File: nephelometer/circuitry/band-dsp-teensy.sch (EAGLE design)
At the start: 23 parts, among them IC1 AD822N, IC4 LM4041CILP, T1 2N2222, T2 2N2222

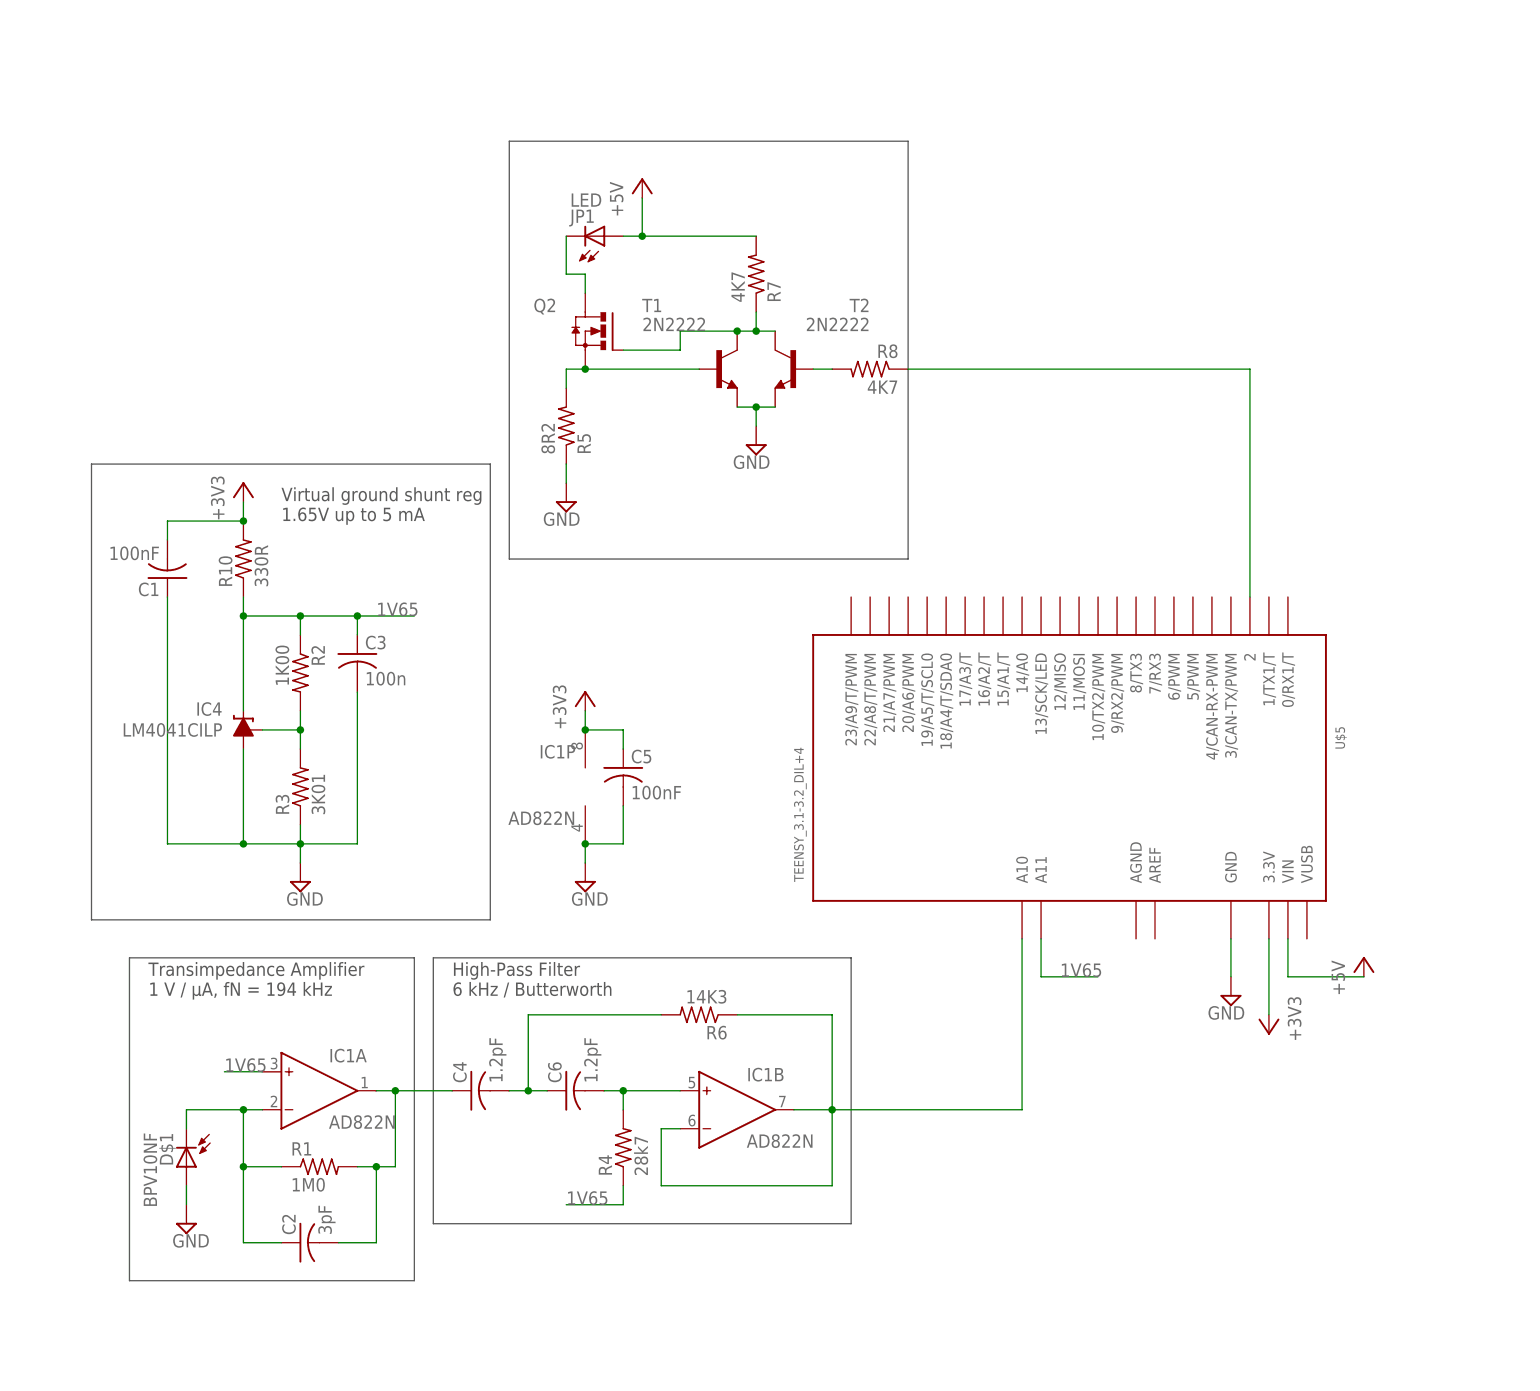
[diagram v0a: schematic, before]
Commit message: programmable gain amplifier incorporated
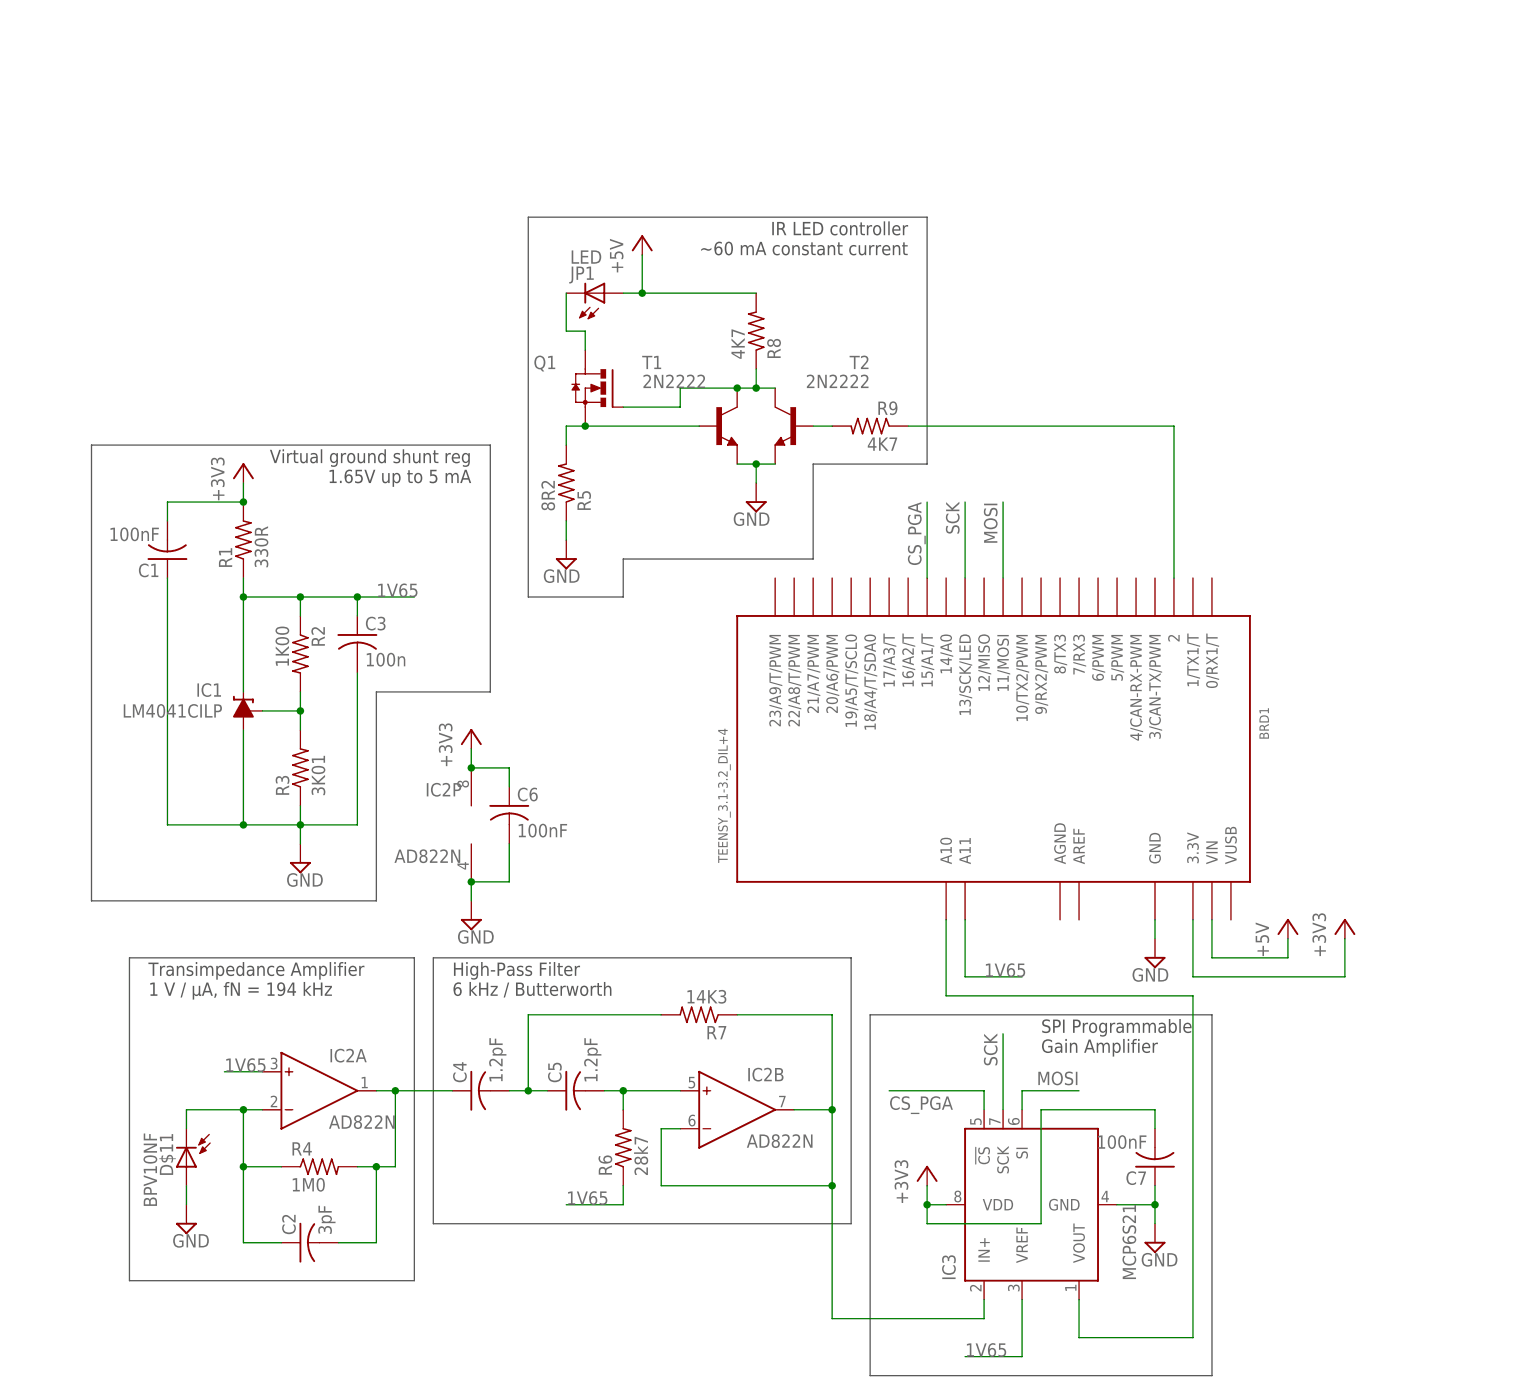
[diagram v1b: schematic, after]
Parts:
- removed IC4: LM4041CILP, texas:LM4041CILP
- removed Q2: (no value), ingolia:IRLB8721
- removed R10: 330R, adafruit:R-US_0207/9
- removed U$5: TEENSY_3.1-3.2_DIL+4, Teensy_3_and_LC_Series_Boards_v1.4:TEENSY_3.1-3.2_DIL+4
- added BRD1: TEENSY_3.1-3.2_DIL+4, Teensy_3_and_LC_Series_Boards_v1.4:TEENSY_3.1-3.2_DIL+4
- added C7: 100nF, adafruit:C-US025-025X050
- added IC2: AD822N, analog-devices:AD822N
- added IC3: MCP6S21, ingolia:MCP6S21
- added Q1: (no value), ingolia:IRLB8721
- added R9: 4K7, adafruit:R-US_0207/9
- C5: value 100nF -> 1.2pF; DIGIKEY# BC1084CT-ND -> BC1026CT-ND; MANF (none) -> Vishay BC Components; MANF# (none) -> K122J15C0GF5TL2
- C6: value 1.2pF -> 100nF; DIGIKEY# BC1026CT-ND -> BC1084CT-ND; MANF Vishay BC Components -> (none); MANF# K122J15C0GF5TL2 -> (none)
- IC1: value AD822N -> LM4041CILP; device analog-devices:AD822N -> texas:LM4041CILP; DIGIKEY# AD823ANZ-ND -> 296-22173-1-ND; MANF Analog Devices Inc. -> Texas Instruments; MANF# AD823ANZ -> LM4041CILPR
- R1: value 1M0 -> 330R; DIGIKEY# RNV14FAL1M00CT-ND -> CF14JT330RCT-ND; MANF Stackpole Electronics Inc -> Stackpole Electronics Inc.; MANF# RNV14FAL1M00 -> CF14JT330R
- R4: value 28k7 -> 1M0; DIGIKEY# 28.7KXBK-ND -> RNV14FAL1M00CT-ND; MANF Yageo -> Stackpole Electronics Inc; MANF# MFR-25FBF52-28K7 -> RNV14FAL1M00
- R6: value 14K3 -> 28k7; DIGIKEY# 14.3KXBK-ND -> 28.7KXBK-ND; MANF# MFR-25FBF52-14K3 -> MFR-25FBF52-28K7
- R7: value 4K7 -> 14K3; DIGIKEY# CF14JT4K70CT-ND -> 14.3KXBK-ND; MANF Stackpole Electronics Inc -> Yageo; MANF# CF14JT4K70 -> MFR-25FBF52-14K3
- renumbered D$1 to D$11
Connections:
- removed net N$10: IC1B.IN-, IC1B.OUT, R6.1, U$5.A10
- new net CS_PGA: BRD1.15/A1/T, IC3.!CS
- new net MOSI: BRD1.11/MOSI, IC3.SI
- new net N$3: IC2B.IN-, IC2B.OUT, IC3.IN+, R7.1
- new net N$4: BRD1.A10, IC3.VOUT
- new net SCK: BRD1.13/SCK/LED, IC3.SCK
- net +3V3: now also BRD1.3.3V, C6.1, C7.2, IC2P.V+, IC3.VDD, R1.2; no longer C5.1, IC1P.V+, R10.2, U$5.3.3V
- net +5V: now also BRD1.VIN, R8.2; no longer R7.2, U$5.VIN
- net 1V65: now also BRD1.A11, IC1.C, IC2A.IN+, IC3.VREF, R1.1, R6.1; no longer IC1A.IN+, IC4.C, R10.1, R4.1, U$5.A11
- net GND: now also BRD1.GND, C6.2, C7.1, IC1.A, IC2P.V-, IC3.GND; no longer C5.2, IC1P.V-, IC4.A, U$5.GND
- net LEDCTRL: now also R9.2; no longer R8.2
- net N$1: now also IC2A.IN-, R4.1; no longer IC1A.IN-, R1.1
- net N$14: now also Q1.S; no longer Q2.S
- net N$18: now also Q1.D; no longer Q2.D
- net N$2: now also C5.1, R7.2; no longer C6.1, R6.2
- net N$22: now also IC2A.OUT, R4.2; no longer IC1A.OUT, R1.2
- net N$35: now also IC1.FB; no longer IC4.FB
- net N$5: now also BRD1.2, R9.1; no longer R8.1, U$5.2
- net N$8: now also Q1.G, R8.1; no longer Q2.G, R7.1
- net N$9: now also C5.2, IC2B.IN+, R6.2; no longer C6.2, IC1B.IN+, R4.2
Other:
- note added: "IR LED controller ~60 mA constant current"
- note added: "SPI Programmable Gain Amplifier"
- moved on the sheet: C1, C3, C5, C6, JP1, R1, R2, R3, R4, R5, R6, R7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

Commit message: Stackable motor controller board w/ 3.3V control; USB versus wall power; test order for components
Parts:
- added D1, D2: 1N5817-T, diode:1N5817-T
- added J1: RJ11-6PTH, SparkFun-Connectors:RJ11-6PTH
- added R10, R11: 330R, adafruit:R-US_0207/9
- added R12: 150R, adafruit:R-US_0207/9
- added U$5: LED3MM-BILEV-INDIC, ingolia:LED3MM-BILEV-INDIC
- added U$6: LED3MM-RG-INDIC, ingolia:LED3MM-RG-INDIC
- BRD1: DIGIKEY2# (none) -> 1568-1422-ND; MANF2 (none) -> SparkFun Electronics; MANF2# (none) -> PRT-13925
- C6, C7: MANF (none) -> Vishay BC Components; MANF# (none) -> K104K15X7RF5TL2
- IC3: DIGIKEY# MCP6S21-I/P-ND -> MCP6S91-E/P-ND; MANF# MCP6S21-I/P -> MCP6S91-E/P
- Q1: value (none) -> IRLB8721
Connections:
- new net MOT1: BRD1.16/A2/T, J1.4
- new net MOT2: BRD1.17/A3/T, J1.3
- new net N$10: D2.A, J1.5, U$6.GA
- new net N$11: R12.2, U$5G$2.A
- new net N$12: R11.2, U$6.GK
- new net N$7: R10.2, U$5G$1.K
- new net V+: BRD1.VUSB, D1.A
- net +3V3: now also R12.1
- net +5V: now also D1.C, D2.C, U$5G$1.A
- net GND: now also J1.2, R10.1, R11.1
- net N$5: now also U$5G$2.K

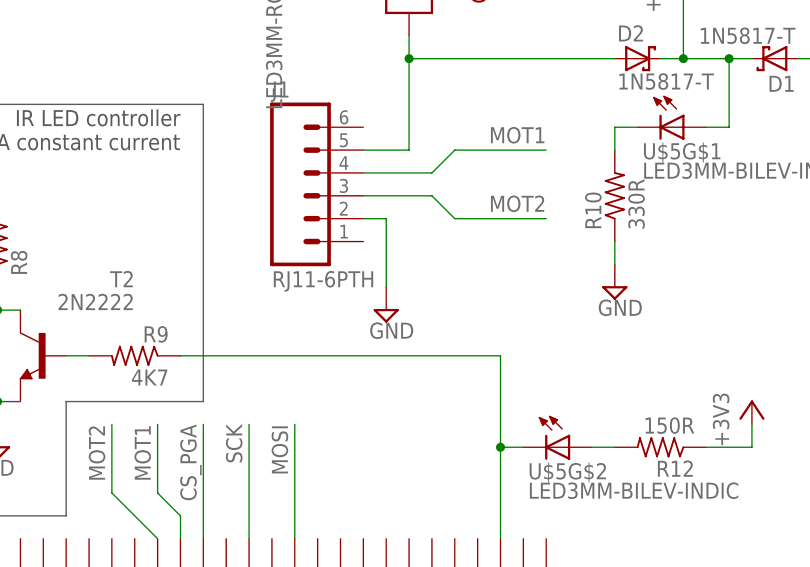
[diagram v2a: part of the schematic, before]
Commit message: Laid out circuit for teensy nephelometer
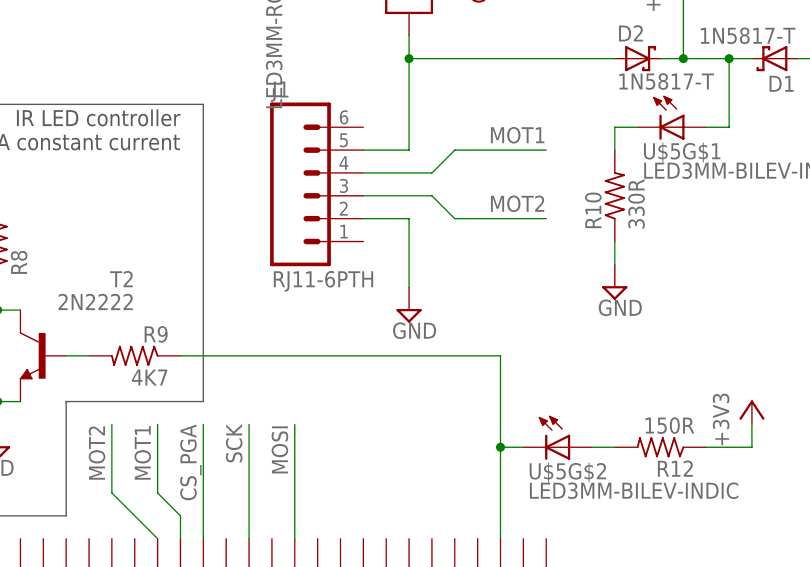
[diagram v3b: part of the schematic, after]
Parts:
- JP1: device ingolia:LED_CXN -> ingolia:1X02_3.5MM_LED
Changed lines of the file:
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@@
 <?xml version="1.0" encoding="utf-8"?>
 <!DOCTYPE eagle SYSTEM "eagle.dtd">
-<eagle version="7.7.0">
+<eagle version="7.5.0">
 <drawing>
 <settings>
@@
 </part>
 <part name="SUPPLY3" library="supply2" deviceset="GND" device=""/>
-<part name="JP1" library="ingolia" deviceset="LED_CXN" device="" value="LED">
+<part name="JP1" library="ingolia" deviceset="1X02_3.5MM_LED" device="" value="LED">
 <attribute name="DIGIKEY#" value="475-3002-ND"/>
 <attribute name="DIGIKEY2#" value="492-1502-ND"/>
@@
 <attribute name="MANF#" x="190.5" y="154.94" size="1.778" layer="96" display="off"/>
 </instance>
-<instance part="SUPPLY10" gate="GND" x="198.12" y="142.24"/>
+<instance part="SUPPLY10" gate="GND" x="200.66" y="142.24"/>
 <instance part="D1" gate="G$1" x="241.3" y="170.18" rot="R180">
 <attribute name="DIGIKEY#" x="241.3" y="170.18" size="1.778" layer="96" rot="R180" display="off"/>
@@
 <segment>
 <pinref part="J1" gate="G$1" pin="2"/>
-<wire x1="195.58" y1="152.4" x2="198.12" y2="152.4" width="0.1524" layer="91"/>
-<wire x1="198.12" y1="152.4" x2="198.12" y2="144.78" width="0.1524" layer="91"/>
+<wire x1="195.58" y1="152.4" x2="200.66" y2="152.4" width="0.1524" layer="91"/>
+<wire x1="200.66" y1="152.4" x2="200.66" y2="144.78" width="0.1524" layer="91"/>
 <pinref part="SUPPLY10" gate="GND" pin="GND"/>
 </segment>
